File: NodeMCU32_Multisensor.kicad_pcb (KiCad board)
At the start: 2 copper layers, 22 parts, among them J1 DHT22, J3 PIR Sensor (HC-SR505), J4 Feuchtesensor, J5 Pumpe, J6 Screw_Terminal_01x02, K1 SRD-05VDC-SL-C, Q1 BC547, U1 ESP32-DEVKITC-32D, U2 HC-SR04

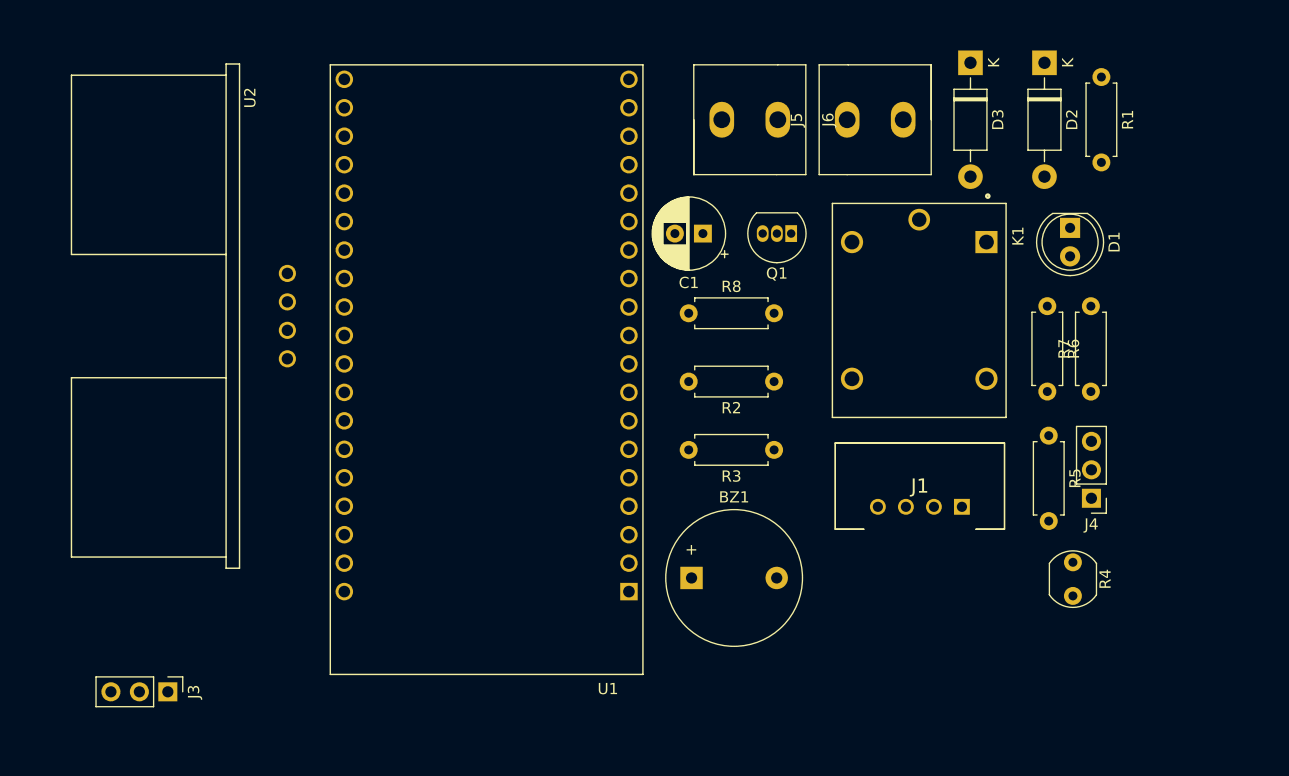
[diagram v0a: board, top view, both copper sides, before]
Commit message: added sensors, finished schematics yet
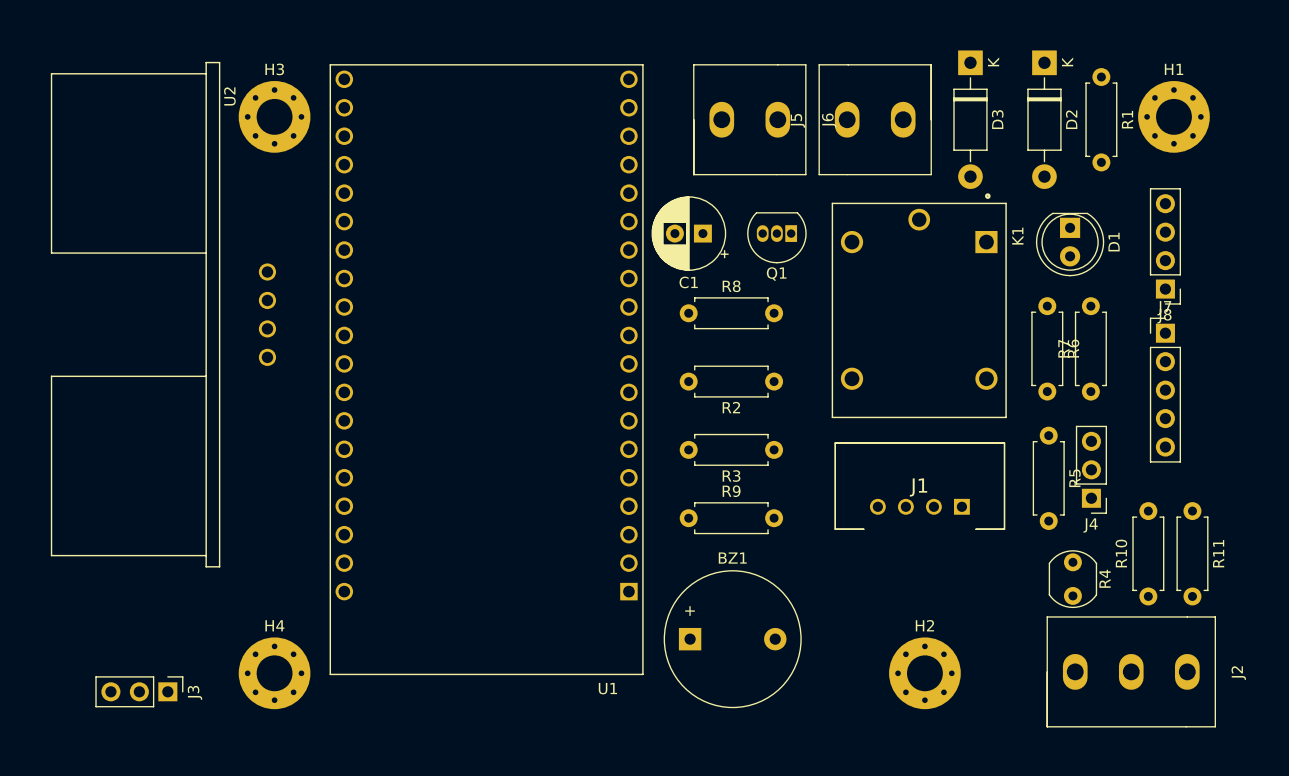
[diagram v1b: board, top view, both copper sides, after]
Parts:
- added H1: MountingHole_Pad, MountingHole:MountingHole_3.2mm_M3_Pad_Via, F.Cu at (149.0, 65.8)
- added H2: MountingHole_Pad, MountingHole:MountingHole_3.2mm_M3_Pad_Via, F.Cu at (126.7, 115.4)
- added H3: MountingHole_Pad, MountingHole:MountingHole_3.2mm_M3_Pad_Via, F.Cu at (68.7, 65.8)
- added H4: MountingHole_Pad, MountingHole:MountingHole_3.2mm_M3_Pad_Via, F.Cu at (68.7, 115.4)
- added J2: LED, TerminalBlock:ScrewTerminal_1x3_P5.00, F.Cu at (155.2, 115.3)
- added J7: Conn_01x05_Male, Connector_PinHeader_2.54mm:PinHeader_1x05_P2.54mm_Vertical, F.Cu at (148.2, 85.1)
- added J8: Conn_01x04_Male, Connector_PinHeader_2.54mm:PinHeader_1x04_P2.54mm_Vertical, F.Cu at (148.2, 81.2)
- added R10: 3400, Resistor_THT:R_Axial_DIN0207_L6.3mm_D2.5mm_P7.62mm_Horizontal, F.Cu at (146.7, 108.6)
- added R11: 5100, Resistor_THT:R_Axial_DIN0207_L6.3mm_D2.5mm_P7.62mm_Horizontal, F.Cu at (150.6, 101.0)
- added R9: 470, Resistor_THT:R_Axial_DIN0207_L6.3mm_D2.5mm_P7.62mm_Horizontal, F.Cu at (105.7, 101.6)
- moved BZ1 5.46 mm to (105.8, 112.4)
- moved U2 1.78 mm to (68.1, 83.4)
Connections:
- R8 pad 2: ESP.17-Pumpe -> ESP.12-Pumpe
- U1 pad 12: Net-(U1-Pad12) -> ESP.14-NeopixelLED
- U1 pad 13: Net-(U1-Pad13) -> ESP.12-Pumpe
- U1 pad 15: Net-(U1-Pad15) -> ESP.13-DigGas
- U1 pad 30: ESP.17-Pumpe -> ESP.17-SDA
- U1 pad 31: Net-(U1-Pad31) -> ESP.16-SCL
- U1 pad 7: Net-(U1-Pad7) -> ESP.32-AnaGas

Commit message: finished pcb layout. check needed.
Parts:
- J7: footprint Connector_PinHeader_2.54mm:PinHeader_1x05_P2.54mm_Vertical -> TerminalBlock:ScrewTerminal_1x5_P5.00
- moved J8 12.6 mm to (142.9, 69.7)
- moved J7 12.2 mm to (150.0, 73.0)
- moved J3 6.14 mm to (53.8, 114.0), turned to 90 degrees
- moved R1 4.06 mm to (138.4, 62.2)
- moved D2 2.79 mm to (134.6, 61.0)
- moved J2 0.35 mm to (154.8, 115.3)
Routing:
- net +3V3: track 0.00 -> 175.0 mm, vias 0 -> 2
- net +5V: track 0.00 -> 154.9 mm
- net ESP.18-LED: track 0.00 -> 96.4 mm, vias 0 -> 1
- net ESP.17-SDA: track 0.00 -> 87.6 mm
- net ESP.13-DigGas: track 0.00 -> 78.7 mm, vias 0 -> 4
- net ESP.16-SCL: track 0.00 -> 76.2 mm
- net ESP.32-AnaGas: track 0.00 -> 66.0 mm, vias 0 -> 1
- net ESP.23-DHT22: track 0.00 -> 63.2 mm, vias 0 -> 1
- net ESP.35-Helligkeitssensor: track 0.00 -> 49.6 mm, vias 0 -> 2
- net ESP.34-Feuchtesensor: track 0.00 -> 47.6 mm, vias 0 -> 1
- net Net-(J8-Pad2): track 0.00 -> 46.7 mm
- net Net-(J2-Pad1): track 0.00 -> 46.7 mm
- net ESP.5-Buzzer: track 0.00 -> 32.4 mm
- net ESP.19-Bewegungsmelder: track 0.00 -> 31.4 mm, vias 0 -> 1
- net Net-(D2-Pad2): track 0.00 -> 28.5 mm
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- added copper zone on B.Cu, net GND
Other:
- board outline added: 111 x 64.9 mm
- board text added: "100"
- board text added: "10K"
- board text added: "2K"
- board text added: "3.4K"
- board text added: "3K"
- board text added: "3V3"
- board text added: "4.7K"
- board text added: "470"
- board text added: "5.1K"
- board text added: "5V"
- board text added: "Buzzer"
- board text added: "DHT22"
- board text added: "Designed by Dirk & Björn Ellwert"
- board text added: "Ech"
- board text added: "GND"
- board text added: "Gas-Sen"
- board text added: "I2C"
- board text added: "INPUT"
- board text added: "M"
- board text added: "Motion detector"
- board text added: "Pump"
- board text added: "S"
- board text added: "SA"
- board text added: "SCL"
- board text added: "SD"
- board text added: "SDA"
- board text added: "Soil Moisture"
- board text added: "Trig"
- board text added: "US-Sen"
- board text added: "↑USB↑"

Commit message: changed pcb layout, yet not finished
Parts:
- renumbered J8 to Je
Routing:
- net ESP.32-AnaGas: track 66.0 -> 64.2 mm
- net +3V3: track 175.0 -> 176.1 mm
- net ESP.13-DigGas: track 78.7 -> 77.8 mm
- net ESP.21-Ulrtasonic.Echo: track 17.8 -> 17.3 mm
